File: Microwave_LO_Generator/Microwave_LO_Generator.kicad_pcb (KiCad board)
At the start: 4 copper layers, 53.3 x 42.9 mm, 76 parts, among them J1 Conn_01x02_Male, J2 Conn_01x02_Male, J3 Conn_01x02_Female, J4 Conn_01x05_Male, J5 Conn_01x02_Female, U1 ADF4150HV, U2 LT1962-3.3, U3 LT3010, U4 HMC739LP4E, U5 LT1962-5, U6 LT1962-5, X1 IQXT-220-1

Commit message: Update
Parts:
- added R21: 100r, Microwave_LO_Generator:R_0201_0603_HandSolder_mod, F.Cu at (112.3, 97.3)
- R14: value 51r -> 100r; footprint Resistor_SMD:R_0402_1005Metric_Pad0.72x0.64mm_HandSolder -> Microwave_LO_Generator:R_0201_0603_HandSolder_mod
- moved C7 5.20 mm to (113.9, 101.6)
- moved R14 3.59 mm to (112.3, 99.1), turned to 270 degrees
- moved TP4 3.56 mm to (137.9, 87.1)
- moved TP2 3.01 mm to (117.5, 115.6)
- moved TP6 2.34 mm to (109.2, 88.2)
- moved J5 1.96 mm to (139.8, 99.9)
- moved R7 1.81 mm to (134.0, 104.5)
- moved C8 1.75 mm to (112.5, 100.6), turned to 180 degrees
- moved R15 1.72 mm to (134.9, 103.2)
- moved R9 1.72 mm to (133.1, 103.2)
- moved C30 1.55 mm to (135.1, 96.0)
- moved C26 1.41 mm to (130.6, 101.3)
- moved C29 0.64 mm to (135.1, 97.0)
- moved J3 0.56 mm to (134.1, 119.7)
- moved C27 0.36 mm to (129.5, 102.5)
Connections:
- U4 pad 1: (no net) -> 0
- U4 pad 12: (no net) -> 0
- U4 pad 13: (no net) -> 0
- U4 pad 14: (no net) -> 0
- U4 pad 18: (no net) -> 0
- U4 pad 19: (no net) -> 0
- U4 pad 21: (no net) -> 0
- U4 pad 23: (no net) -> 0
- U4 pad 24: (no net) -> 0
- U4 pad 3: (no net) -> 0
- U4 pad 5: (no net) -> 0
- U4 pad 6: (no net) -> 0
- U4 pad 7: (no net) -> 0
- U4 pad 8: (no net) -> 0
- U4 pad 9: (no net) -> 0
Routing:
- net 0: track 61.3 -> 280.8 mm, vias 147 -> 281
- net +3V3: track 109.1 -> 134.6 mm
- net DIV16: track 6.55 -> 8.17 mm
- net Net-(J5-Pad1): track 5.42 -> 4.13 mm
- net Net-(J3-Pad1): track 14.9 -> 14.2 mm
- net Net-(R15-Pad1): track 4.68 -> 3.96 mm
- net +5VD: track 17.5 -> 16.9 mm
- net +6V: track 137.0 -> 136.5 mm
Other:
- board size 53.3 x 42.9 mm -> 49.7 x 41.9 mm

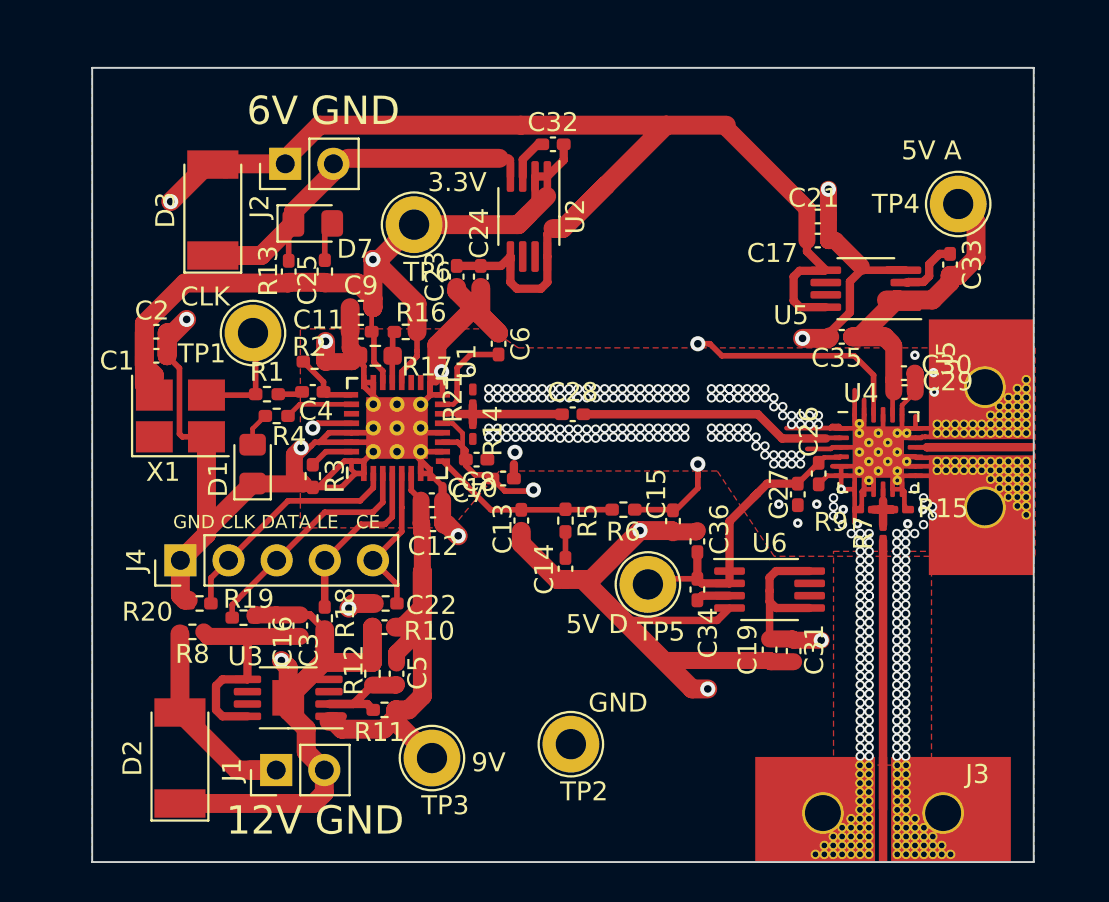
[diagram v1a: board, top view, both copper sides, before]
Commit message: Add stability hole
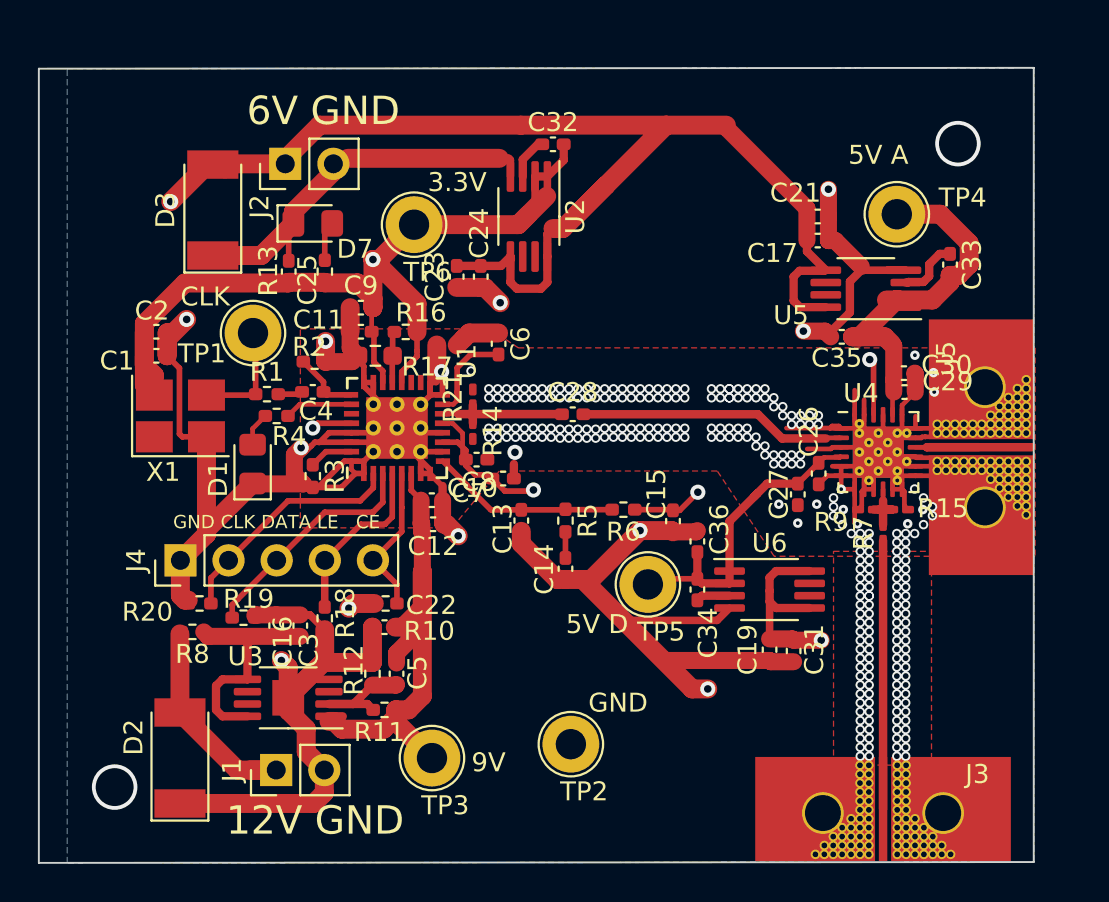
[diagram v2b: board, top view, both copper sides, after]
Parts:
- moved TP4 3.28 mm to (134.7, 87.7)
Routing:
- net 0: track 280.8 -> 276.9 mm, vias 281 -> 284
- net CPout: track 24.2 -> 22.2 mm
- net +5VA: track 19.0 -> 20.9 mm
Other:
- board size 49.7 x 41.9 mm -> 52.5 x 42 mm

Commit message: Edit annular ring
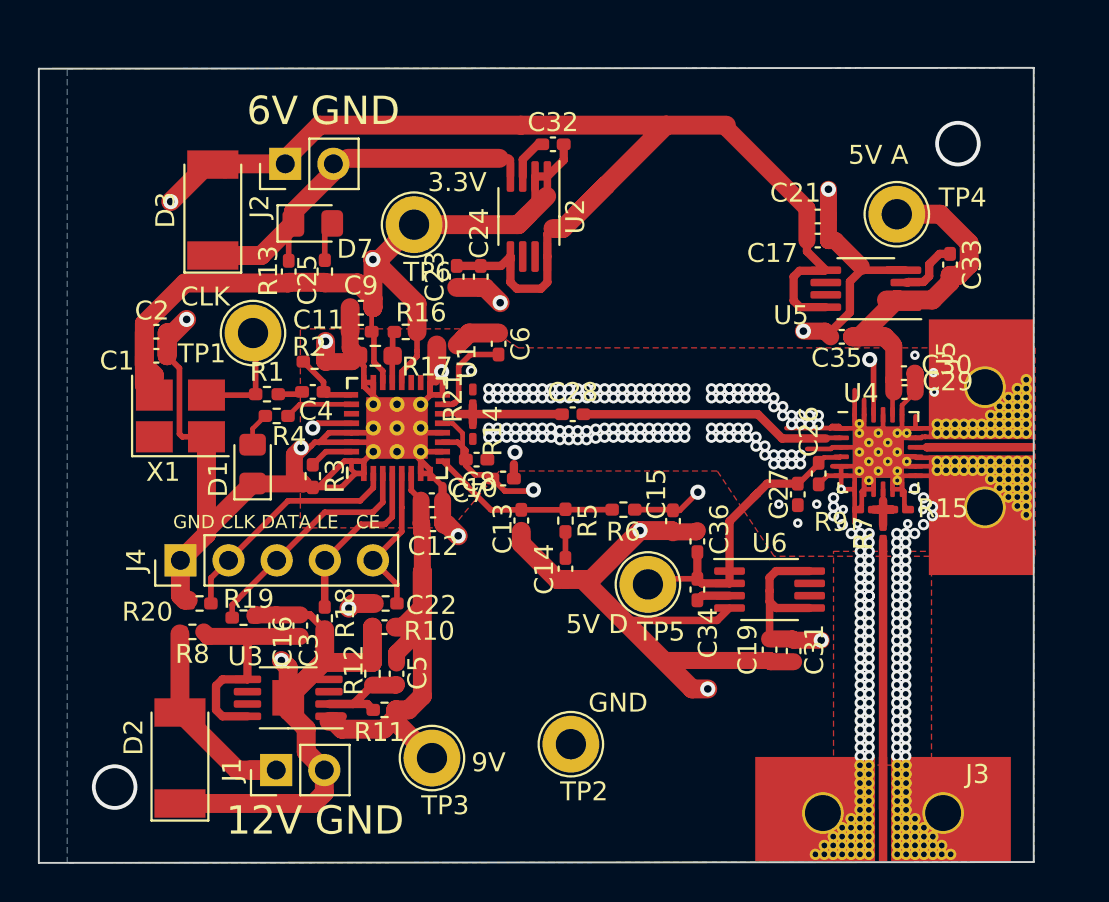
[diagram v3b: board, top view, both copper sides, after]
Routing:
- net +3V3: track 134.6 -> 127.7 mm

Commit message: update
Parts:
- removed R17: DNI, Resistor_SMD:R_0603_1608Metric_Pad0.98x0.95mm_HandSolder
- moved C11 1.58 mm to (106.8, 95.4)
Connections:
- U1 pad 18: (no net) -> Net-(U1-Pad18)
- U1 pad 19: (no net) -> Net-(U1-Pad19)
- U1 pad 27: (no net) -> Net-(U1-Pad27)
- U2 pad 6: (no net) -> Net-(U2-Pad6)
- U2 pad 7: (no net) -> Net-(U2-Pad7)
- U3 pad 3: (no net) -> Net-(U3-Pad3)
- U3 pad 6: (no net) -> Net-(U3-Pad6)
- U3 pad 7: (no net) -> Net-(U3-Pad7)
- U5 pad 6: (no net) -> Net-(U5-Pad6)
- U5 pad 7: (no net) -> Net-(U5-Pad7)
- U6 pad 6: (no net) -> Net-(U6-Pad6)
- U6 pad 7: (no net) -> Net-(U6-Pad7)
- X1 pad 1: (no net) -> Net-(X1-Pad1)
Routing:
- net +3V3: track 127.7 -> 128.4 mm

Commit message: some_update
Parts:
- removed R16: 0, Resistor_SMD:R_0402_1005Metric_Pad0.72x0.64mm_HandSolder
- moved C9 1.82 mm to (106.5, 94.4)
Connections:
- U1 pad 21: Net-(R16-Pad2) -> +3V3
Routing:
- net +3V3: track 128.4 -> 123.9 mm
- net Net-(R16-Pad2): track 2.74 -> 0.00 mm
- net 0: track 276.5 -> 275.3 mm
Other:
- board size 52.5 x 42 mm -> 52.5 x 41.9 mm

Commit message: backup
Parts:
- C28: footprint Capacitor_SMD:C_0402_1005Metric_Pad0.74x0.62mm_HandSolder -> Capacitor_SMD:C_0201_0603Metric_Pad0.64x0.40mm_HandSolder

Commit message: update bom
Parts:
- renumbered C12 to C10, C13 to C11, C14 to C12, C15 to C13, C16 to C14, C3 to C15, C5 to C16, C22 to C17, C23 to C18, C17 to C19, C19 to C20, C24 to C21, C21 to C22, C31 to C23, C32 to C24, C33 to C25, C34 to C26, C25 to C27, C35 to C28, C36 to C29, C4 to C3, C27 to C30, C26 to C31, C28 to C32, C29 to C33, C30 to C34, C6 to C4, C7 to C5, C8 to C6, C9 to C7, C10 to C8, C11 to C9, D7 to D4, J4 to J1, J1 to J2, J2 to J3, J3 to J4, R10 to R1, R6 to R10, R8 to R11, R11 to R12, R12 to R13, R13 to R14, R14 to R15, R7 to R16, R21 to R17, R9 to R18, R15 to R19, R1 to R2, R18 to R3, R19 to R4, R20 to R5, R2 to R6, R3 to R7, R4 to R8, R5 to R9, U3 to U2, U2 to U3, U5 to U4, U6 to U5, U4 to U6

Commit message: solder clearence + gerber
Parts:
- J4, J5: footprint Microwave_LO_Generator:Connettore -> Microwave_LO_Generator:Connettore_largo
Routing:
- net +3V3: track 123.9 -> 124.9 mm
- net 0: vias 284 -> 285
- net (no net): vias 0 -> 2
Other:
- rule pad_to_mask_clearance: 0 -> 0.2
